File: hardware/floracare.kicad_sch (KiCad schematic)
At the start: 15 parts, among them J1 USB_C_Receptacle_USB2.0_14P, J2 Conn_01x04_Socket, J4 Conn_01x04_Socket, J5 Conn_01x14_Socket, J6 Conn_01x05_Socket, U1 AMS1117-3.3, U2 ESP32-S3-WROOM-1

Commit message: Update global pcb
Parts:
- removed J1: USB_C_Receptacle_USB2.0_14P, Connector_USB:USB_C_Receptacle_HCTL_HC-TYPE-C-16P-01A, symbol Connector:USB_C_Receptacle_USB2.0_14P
- added J3: USB_C_Receptacle_USB2.0_16P, Connector_USB:USB_C_Receptacle_HCTL_HC-TYPE-C-16P-01A, symbol Connector:USB_C_Receptacle_USB2.0_16P
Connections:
- net +5V: now also J3.A4 (VBUS), J3.A9 (VBUS), J3.B4 (VBUS), J3.B9 (VBUS)
- net DATA+: now also J3.A6 (D+), J3.B6 (D+)
- net DATA-: now also J3.A7 (D-), J3.B7 (D-)
- net GND: now also J3.A1 (GND), J3.A12 (GND), J3.B1 (GND), J3.B12 (GND), J3.S1 (SHIELD)
- net at R2.1: now also J3.A5 (CC1)
- net at R1.1: now also J3.B5 (CC2)
- no-connect marks 34 -> 36
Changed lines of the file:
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@@
+	)
+	(junction
+		(at 45.72 130.81)
+		(diameter 0)
+		(color 0 0 0 0)
+	)
+	(junction
+		(at 45.72 128.27)
+		(diameter 0)
+		(color 0 0 0 0)
+	)
+	(junction
+		(at 46.99 29.21)
+		(diameter 0)
+		(color 0 0 0 0)
+	)
+	(junction
+		(at 45.72 123.19)
+		(diameter 0)
+		(color 0 0 0 0)
+	)
+	(junction
+		(at 99.06 35.56)
+		(diameter 0)
+		(color 0 0 0 0)
 	)
 	(junction
@@
 		(color 0 0 0 0)
 	)
-	(junction
-		(at 45.72 130.81)
-		(diameter 0)
-		(color 0 0 0 0)
-	)
-	(junction
-		(at 46.99 29.21)
-		(diameter 0)
-		(color 0 0 0 0)
-	)
-	(junction
-		(at 45.72 128.27)
-		(diameter 0)
-		(color 0 0 0 0)
-	)
-	(junction
-		(at 45.72 123.19)
-		(diameter 0)
-		(color 0 0 0 0)
-	)
-	(junction
-		(at 99.06 35.56)
-		(diameter 0)
-		(color 0 0 0 0)
-	)
 	(no_connect
 		(at 60.96 157.48)
@@
 	)
 	(no_connect
+		(at 46.99 57.15)
+	)
+	(no_connect
 		(at 195.58 78.74)
 	)
@@
 	(no_connect
 		(at 60.96 172.72)
+	)
+	(no_connect
+		(at 46.99 59.69)
 	)
 	(no_connect
@@
 	)
 	(symbol
-		(lib_id "Connector:USB_C_Receptacle_USB2.0_14P")
-		(at 31.75 44.45 0)
-		(unit 1)
-		(exclude_from_sim no)
-		(in_bom yes)
-		(on_board yes)
-		(dnp no)
-		(property "Reference" "J1"
-			(at 30.226 15.494 0)
-			(effects
-				(font
-					(size 1.27 1.27)
-				)
-			)
-		)
-		(property "Value" "USB_C_Receptacle_USB2.0_14P"
-			(at 30.48 17.526 0)
-			(effects
-				(font
-					(size 1.27 1.27)
-				)
-			)
-		)
-		(property "Footprint" "Connector_USB:USB_C_Receptacle_HCTL_HC-TYPE-C-16P-01A"
-			(at 35.56 44.45 0)
-			(effects
-				(font
-					(size 1.27 1.27)
-				)
-				(hide yes)
-			)
-		)
-		(property "Datasheet" "https://www.usb.org/sites/default/files/documents/usb_type-c.zip"
-			(at 35.56 44.45 0)
-			(effects
-				(font
-					(size 1.27 1.27)
-				)
-				(hide yes)
-			)
-		)
-		(property "Description" "USB 2.0-only 14P Type-C Receptacle connector"
-			(at 31.75 44.45 0)
-			(effects
-				(font
-					(size 1.27 1.27)
-				)
-				(hide yes)
-			)
-		)
-		(pin "B7"
-		)
-		(pin "A9"
-		)
-		(pin "B4"
-		)
-		(pin "A7"
-		)
-		(pin "A12"
-		)
-		(pin "A5"
-		)
-		(pin "S1"
-		)
-		(pin "A1"
-		)
-		(pin "B1"
-		)
-		(pin "B5"
-		)
-		(pin "B12"
-		)
-		(pin "A4"
-		)
-		(pin "A6"
-		)
-		(pin "B6"
-		)
-		(pin "B9"
-		)
-		(instances
-			(project ""
-				(path "/a233d2e6-40a7-473a-8214-598adc2356c8"
-					(reference "J1")
-					(unit 1)
-				)
-			)
-		)
-	)
-	(symbol
 		(lib_id "Connector:Conn_01x04_Socket")
 		(at 248.92 45.72 0)
@@
 					(unit 1)
 				)
+			)
+		)
+	)
+	(symbol
+		(lib_id "Connector:USB_C_Receptacle_USB2.0_16P")
+		(at 31.75 44.45 0)
+		(unit 1)
+		(exclude_from_sim no)
+		(in_bom yes)
+		(on_board yes)
+		(dnp no)
+		(property "Reference" "J3"
+			(at 31.496 18.288 0)
+			(effects
+				(font
+					(size 1.27 1.27)
+				)
+			)
+		)
+		(property "Value" "USB_C_Receptacle_USB2.0_16P"
+			(at 31.496 20.828 0)
+			(effects
+				(font
+					(size 1.27 1.27)
+				)
+			)
+		)
+		(property "Footprint" "Connector_USB:USB_C_Receptacle_HCTL_HC-TYPE-C-16P-01A"
+			(at 35.56 44.45 0)
+			(effects
+				(font
+					(size 1.27 1.27)
+				)
+				(hide yes)
+			)
+		)
+		(property "Datasheet" "https://www.usb.org/sites/default/files/documents/usb_type-c.zip"
+			(at 35.56 44.45 0)
+			(effects
+				(font
+					(size 1.27 1.27)
+				)
+				(hide yes)
+			)
+		)
+		(property "Description" "USB 2.0-only 16P Type-C Receptacle connector"
+			(at 31.75 44.45 0)
+			(effects
+				(font
+					(size 1.27 1.27)
+				)
+				(hide yes)
+			)
+		)
+		(pin "S1"
+		)
+		(pin "A1"
+		)
+		(pin "A4"
+		)
+		(pin "A12"
+		)
+		(pin "B1"
+		)
+		(pin "B12"
+		)
+		(pin "A7"
+		)
+		(pin "A9"
+		)
+		(pin "B5"
+		)
+		(pin "A5"
+		)
+		(pin "B7"
+		)
+		(pin "B4"
+		)
+		(pin "B9"
+		)
+		(pin "B8"
+		)
+		(pin "A8"
+		)
+		(pin "A6"
+		)
+		(pin "B6"
+		)
+		(instances
+			(project ""
+				(path "/a233d2e6-40a7-473a-8214-598adc2356c8"
+					(reference "J3")
+					(unit 1)
+				)

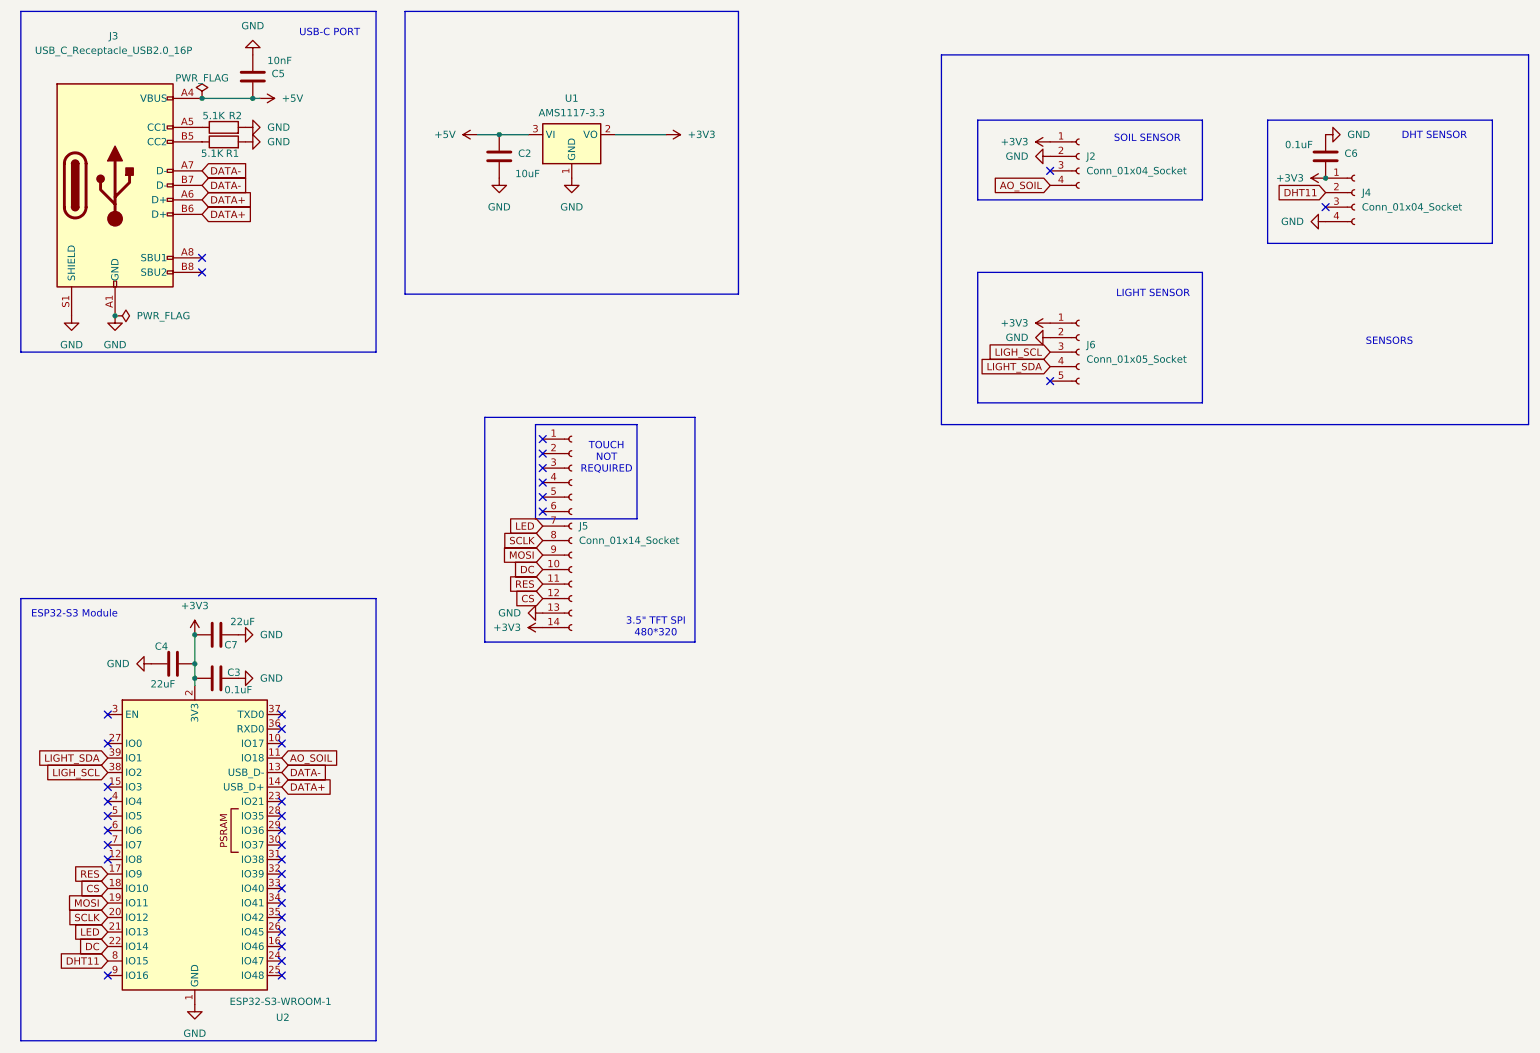
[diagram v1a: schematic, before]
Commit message: Adding EN and BOOT buttons
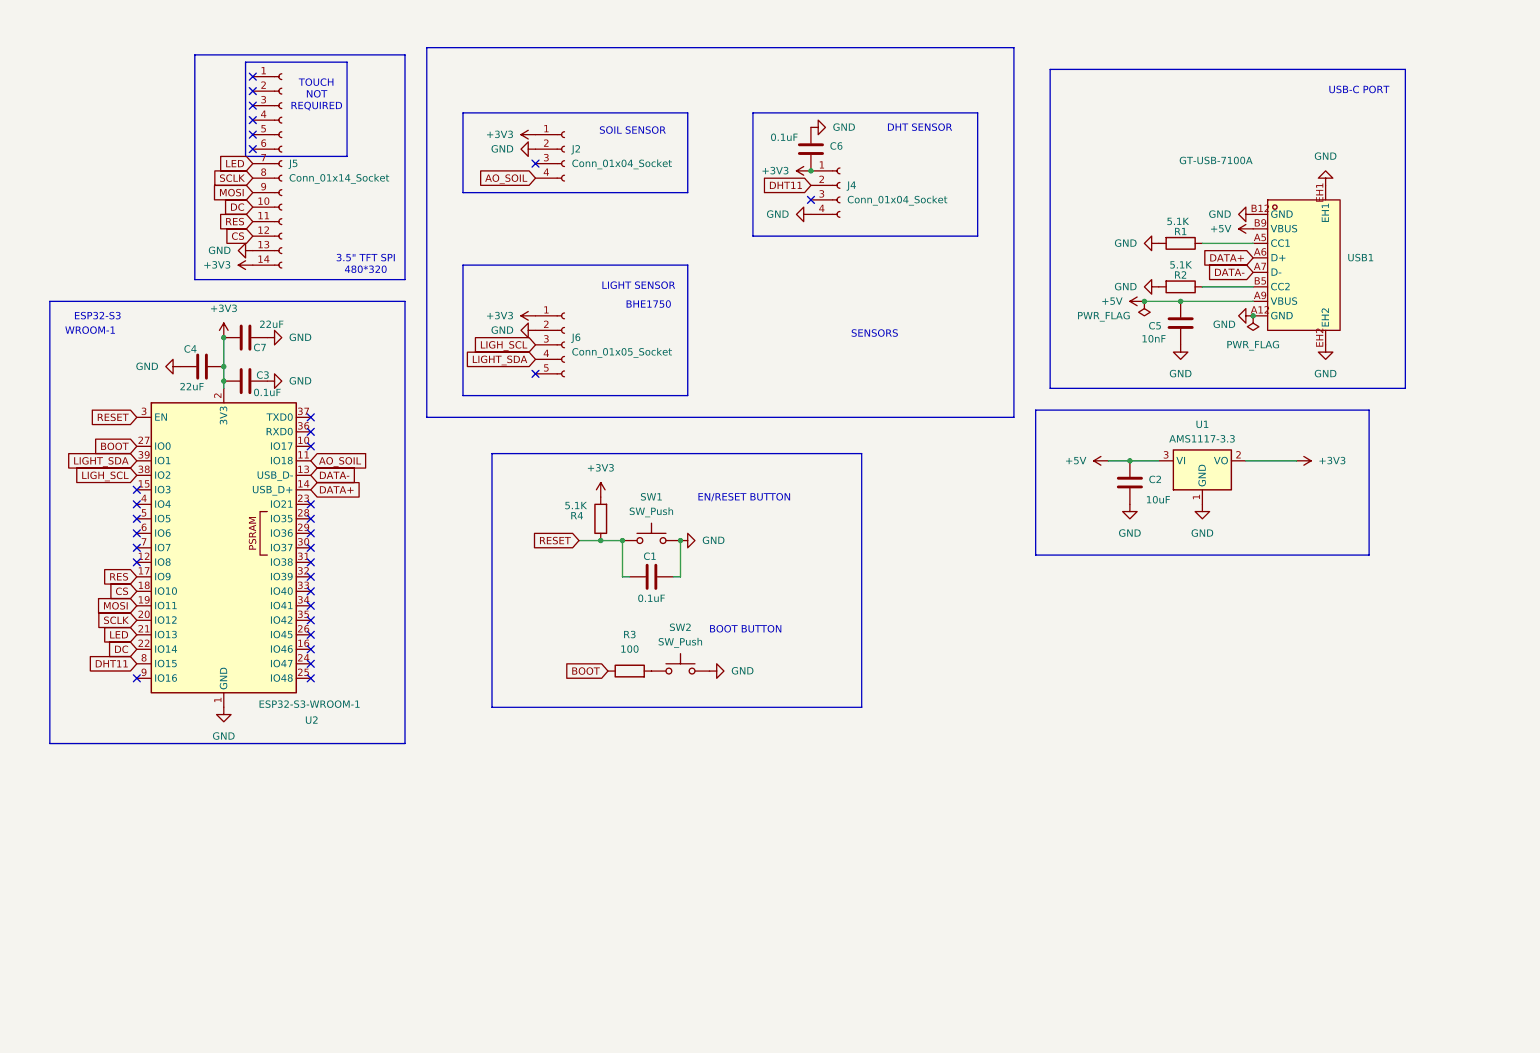
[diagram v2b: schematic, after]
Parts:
- removed J3: USB_C_Receptacle_USB2.0_16P, Connector_USB:USB_C_Receptacle_HCTL_HC-TYPE-C-16P-01A, symbol Connector:USB_C_Receptacle_USB2.0_16P
- added C1: 0.1uF, symbol Device:C
- added R3: 100, symbol Device:R
- added R4: 5.1K, symbol Device:R
- added SW1, SW2: SW_Push, symbol Switch:SW_Push
- added USB1: GT-USB-7100A, easyeda2kicad:USB-C-SMD_GT-USB-7100A, symbol usbeasy:GT-USB-7100A
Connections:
- net +3V3: now also R4.2
- net +5V: now also USB1.A9 (VBUS), USB1.B9 (VBUS)
- net DATA+: now also USB1.A6 (D+)
- net DATA-: now also USB1.A7 (D-)
- net GND: now also C1.2, SW1.2, SW2.2, USB1.A12 (GND), USB1.B12 (GND), USB1.EH1, USB1.EH2
- net at R2.1: now also USB1.B5 (CC2)
- net at R1.1: now also USB1.A5 (CC1)
- net BOOT: now reaches U2.27 (IO0)
- net BOOT: now also R3.1
- net RESET: now reaches U2.3 (EN)
- net RESET: now also C1.1, R4.1, SW1.1
- new net: R3.2, SW2.1
- no-connect marks 36 -> 32
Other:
- note added: "BHE1750"
- note added: "BOOT BUTTON"
- note added: "EN/RESET BUTTON"
- note added: "ESP32-S3"
- note added: "WROOM-1"
- note removed: "ESP32-S3 Module"
- moved on the sheet: C2, C3, C4, C5, C6, C7, J2, J4, J5, J6, U1, U2

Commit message: Updating general Project
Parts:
- C1: footprint (none) -> Capacitor_SMD:C_0805_2012Metric
- R3, R4: footprint (none) -> Resistor_SMD:R_0805_2012Metric_Pad1.20x1.40mm_HandSolder
- SW1, SW2: footprint (none) -> Button_Switch_SMD:SW_SPST_SKQG_WithStem
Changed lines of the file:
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@@
 	(symbol
 		(lib_id "power:GND")
-		(at 130.81 106.68 90)
-		(unit 1)
-		(exclude_from_sim no)
-		(in_bom yes)
-		(on_board yes)
-		(dnp no)
-		(fields_autoplaced yes)
+		(at 130.81 106.68 180)
+		(unit 1)
+		(exclude_from_sim no)
+		(in_bom yes)
+		(on_board yes)
+		(dnp no)
 		(property "Reference" "#PWR06"
-			(at 137.16 106.68 0)
+			(at 130.81 100.33 0)
 			(effects
 				(font
@@
 		)
 		(property "Value" "GND"
-			(at 134.62 106.6799 90)
-			(effects
-				(font
-					(size 1.27 1.27)
-				)
-				(justify right)
+			(at 134.62 103.886 0)
+			(effects
+				(font
+					(size 1.27 1.27)
+				)
 			)
 		)
@@
 			)
 		)
-		(property "Footprint" ""
+		(property "Footprint" "Button_Switch_SMD:SW_SPST_SKQG_WithStem"
 			(at 130.81 124.46 0)
 			(effects
@@
 			)
 		)
-		(property "Footprint" ""
+		(property "Footprint" "Capacitor_SMD:C_0805_2012Metric"
 			(at 129.54 112.0648 0)
 			(effects
@@
 			)
 		)
-		(property "Footprint" ""
+		(property "Footprint" "Resistor_SMD:R_0805_2012Metric_Pad1.20x1.40mm_HandSolder"
 			(at 118.618 102.87 90)
 			(effects
@@
 			)
 		)
-		(property "Footprint" ""
+		(property "Footprint" "Resistor_SMD:R_0805_2012Metric_Pad1.20x1.40mm_HandSolder"
 			(at 121.92 131.318 90)
 			(effects
@@
 			)
 		)
-		(property "Footprint" ""
+		(property "Footprint" "Button_Switch_SMD:SW_SPST_SKQG_WithStem"
 			(at 125.73 101.6 0)
 			(effects

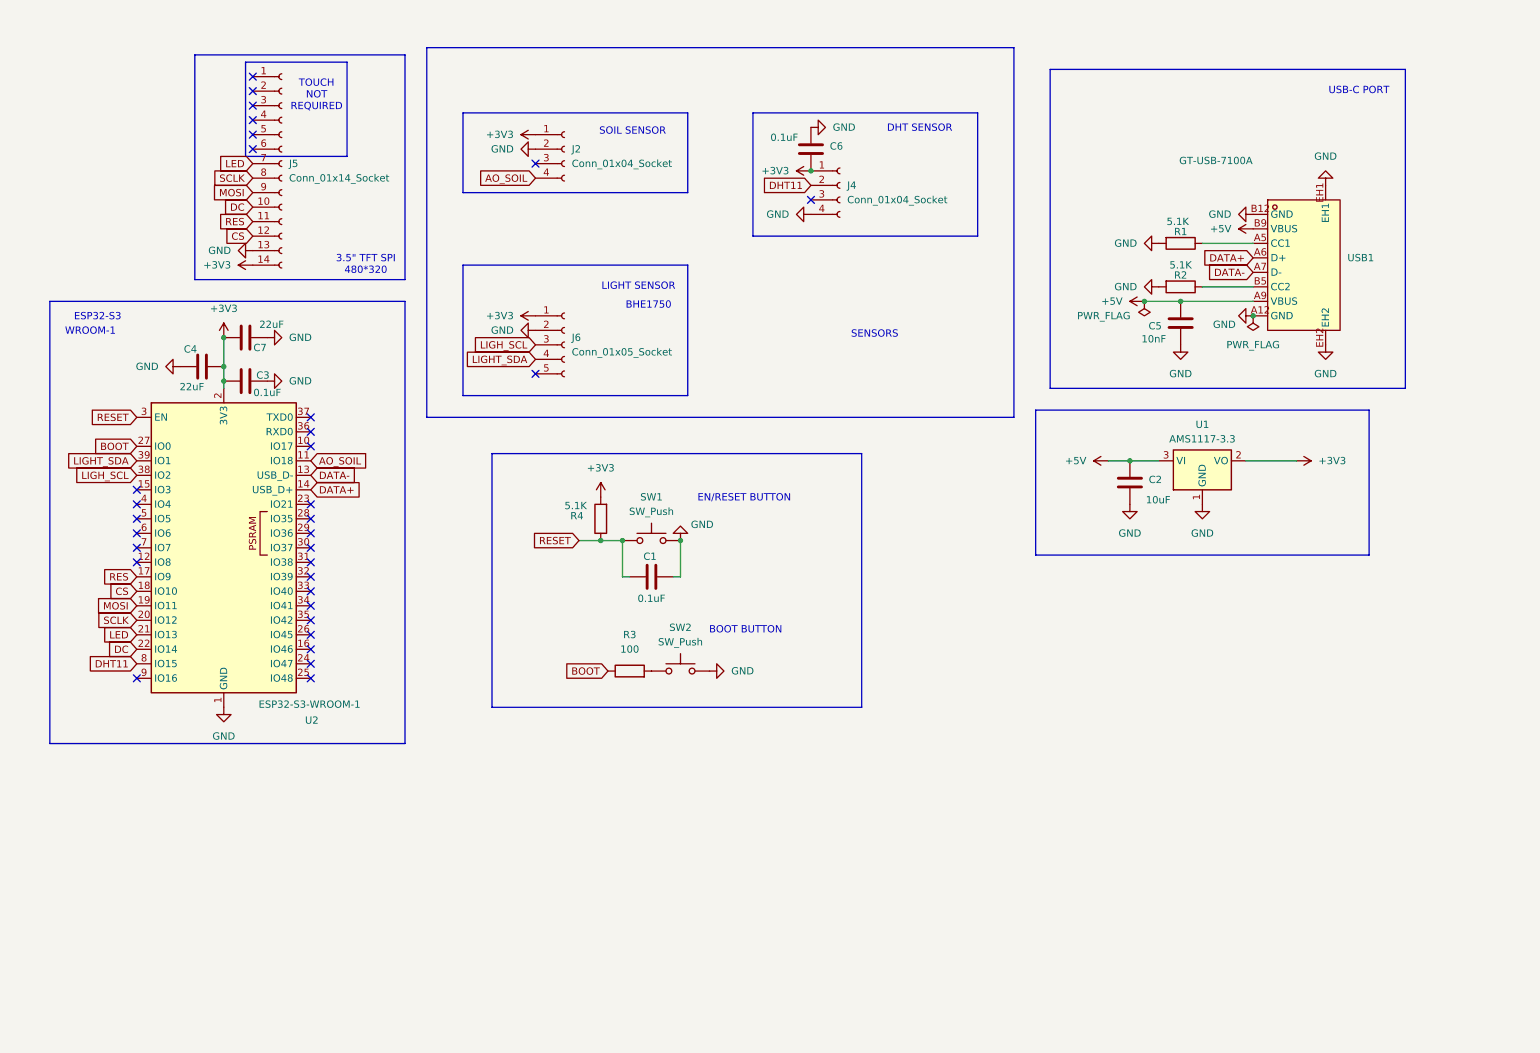
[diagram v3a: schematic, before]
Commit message: Replacing usb slot
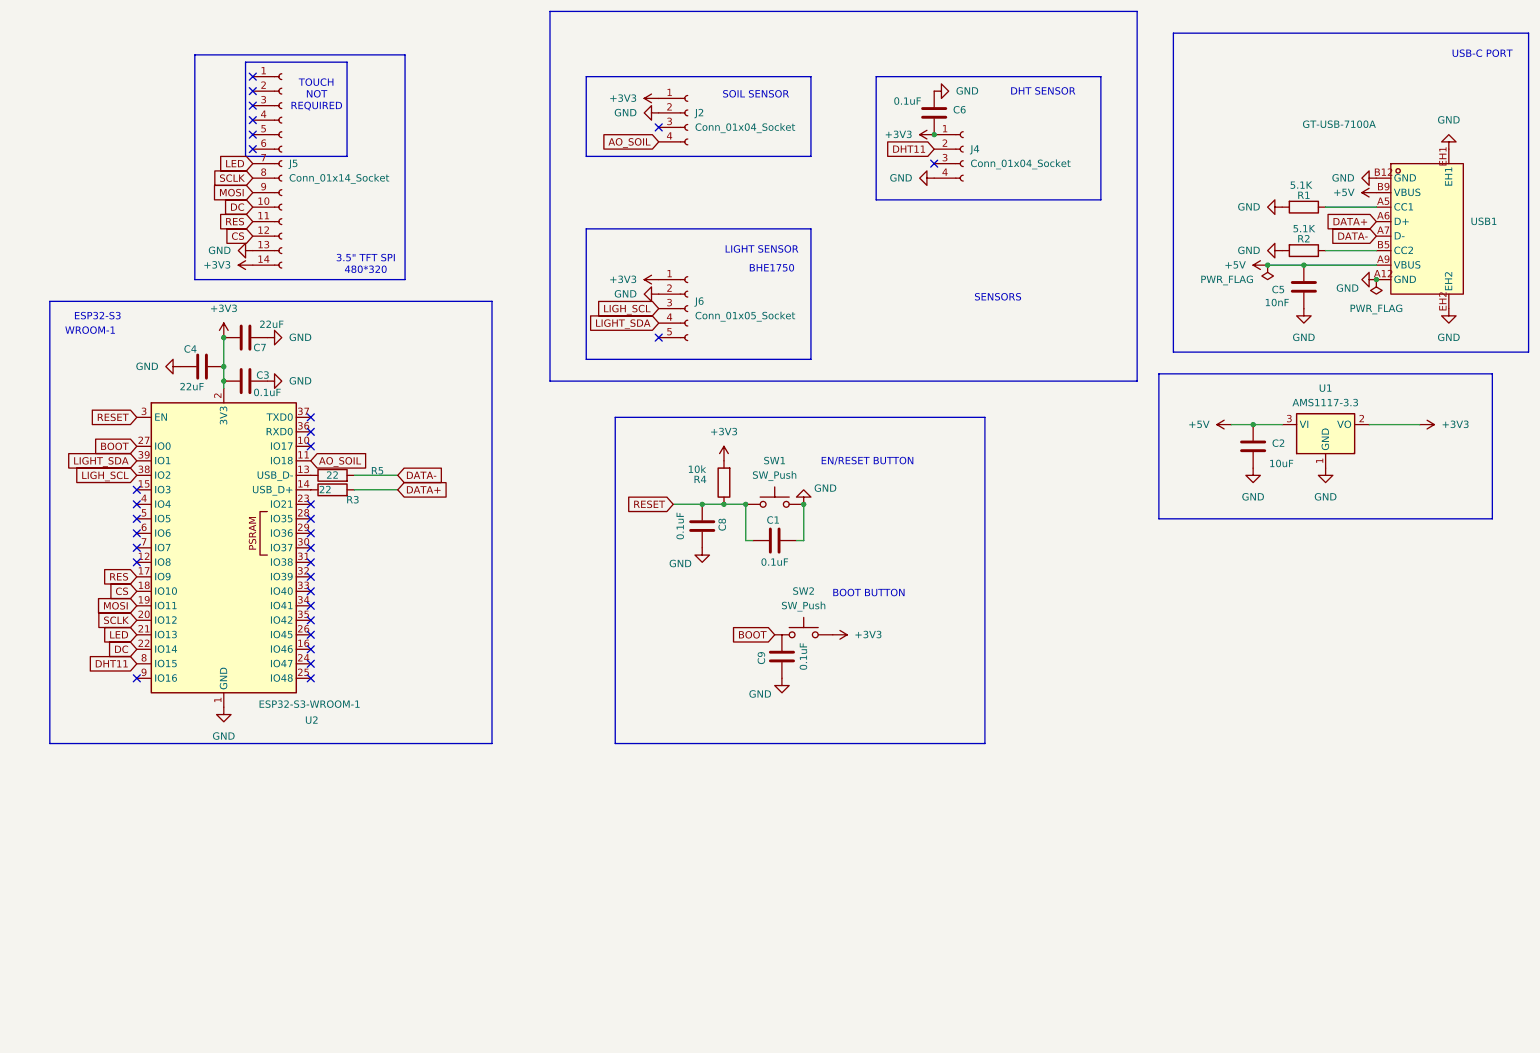
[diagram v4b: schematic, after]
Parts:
- added C8, C9: 0.1uF, Capacitor_SMD:C_0805_2012Metric, symbol Device:C
- added R5: 22, LED_SMD:LED_0805_2012Metric_Pad1.15x1.40mm_HandSolder, symbol Device:R
- R3: value 100 -> 22; footprint Resistor_SMD:R_0805_2012Metric_Pad1.20x1.40mm_HandSolder -> LED_SMD:LED_0805_2012Metric_Pad1.15x1.40mm_HandSolder
- R4: value 5.1K -> 10k
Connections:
- net +3V3: now also SW2.2
- net BOOT: now also SW2.1; no longer R3.1
- net DATA+: now also R3.2; no longer U2.14 (USB_D+)
- net DATA-: now also R5.2; no longer U2.13 (USB_D-)
- net GND: now also C8.2, C9.1; no longer SW2.2
- net RESET: now also C8.1
- new net: R5.1, U2.13 (USB_D-)
- new net: R3.1, U2.14 (USB_D+)
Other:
- moved on the sheet: C1, C2, C5, C6, J2, J4, J6, R1, R2, R4, SW1, SW2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
